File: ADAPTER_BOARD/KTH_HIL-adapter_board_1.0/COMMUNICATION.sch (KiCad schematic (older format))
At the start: 15 parts, among them U1 SN65HVD233, U2 SN65HVD233

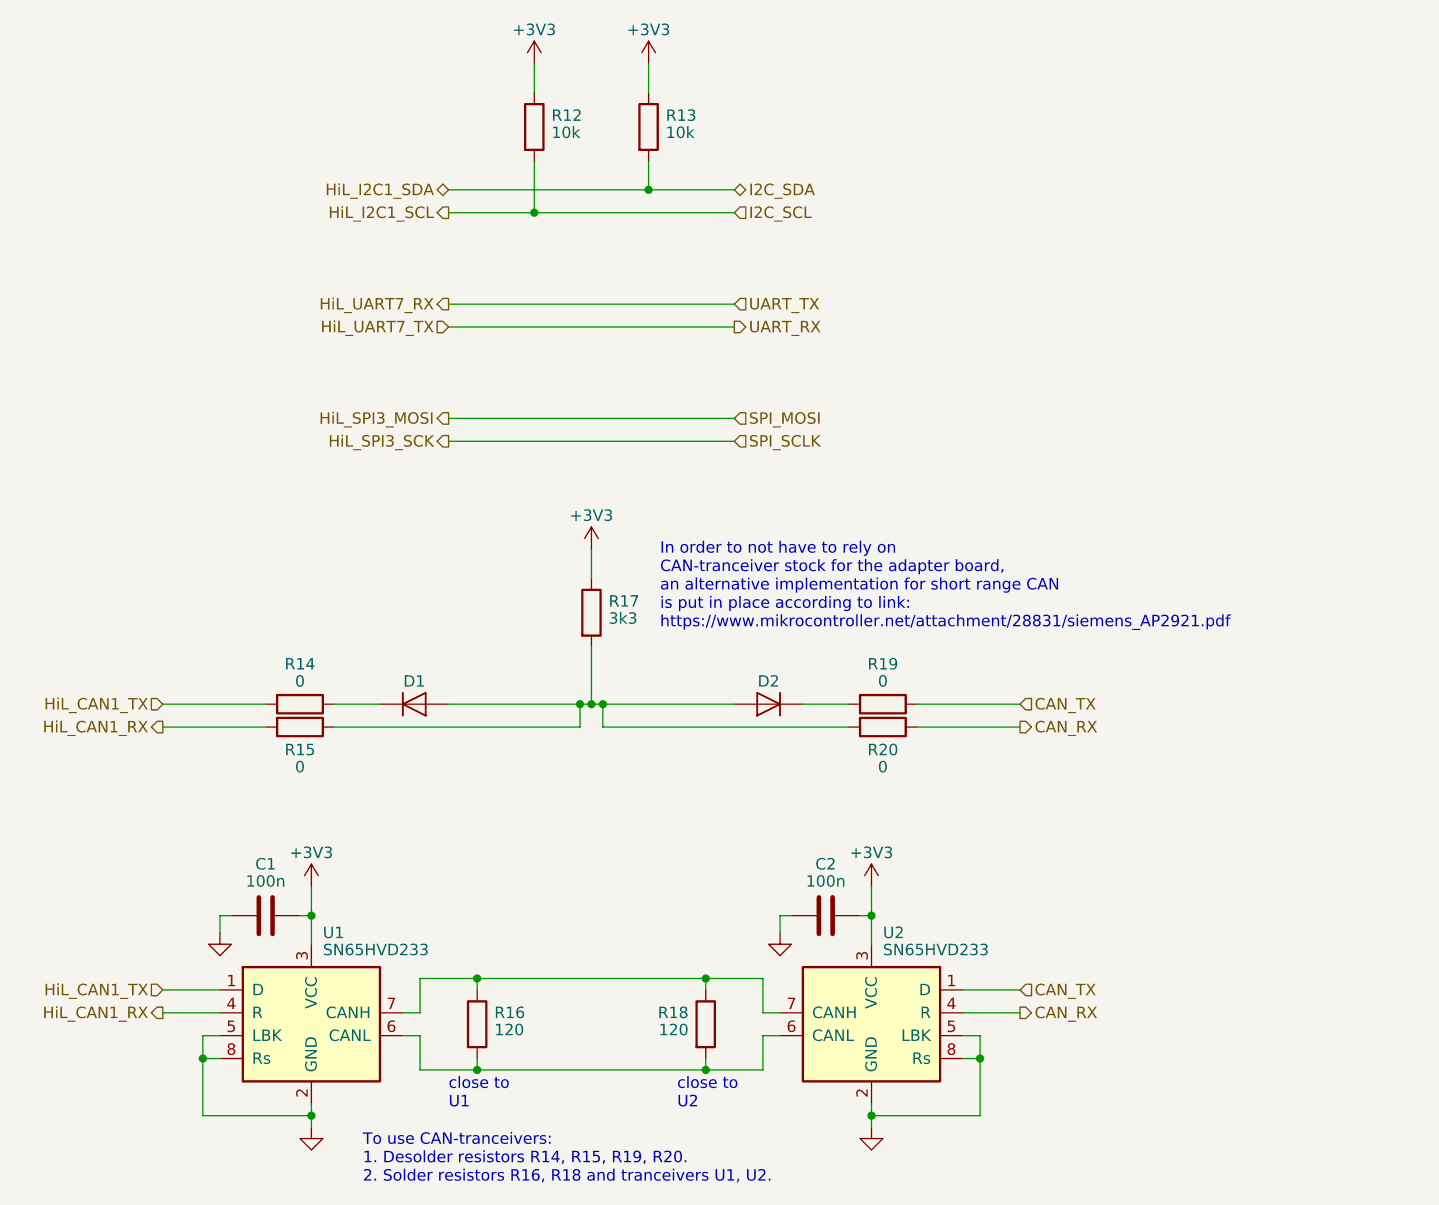
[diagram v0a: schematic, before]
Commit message: Fixed comments regarding schematic
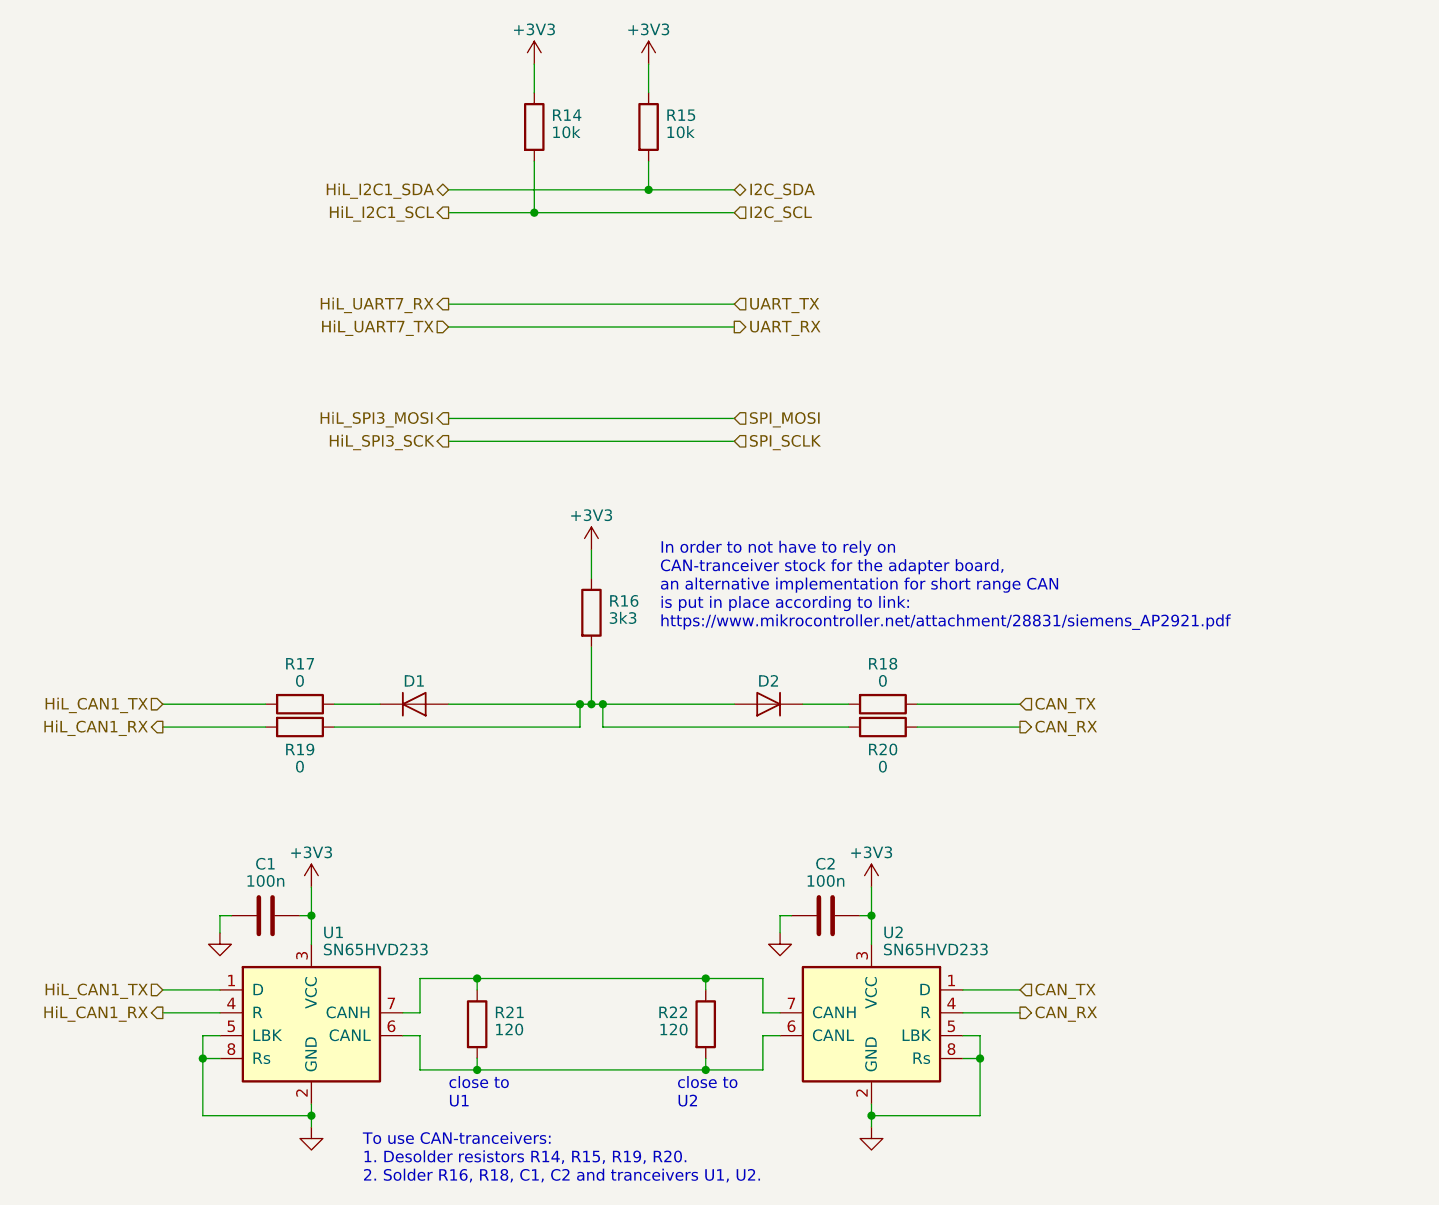
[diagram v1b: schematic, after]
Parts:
- renumbered R12 to R14, R13 to R15, R17 to R16, R14 to R17, R19 to R18, R15 to R19, R16 to R21, R18 to R22
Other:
- note added: "To use CAN-tranceivers:\n1. Desolder resistors R14, R15, R19, R20. \n2. Solder R16, R18, C1, C2 and tranceivers U1, U2."
- note removed: "To use CAN-tranceivers:\n1. Desolder resistors R14, R15, R19, R20. \n2. Solder resistors R16, R18 and tranceivers U1, U2."
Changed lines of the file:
@@
 EESchema Schematic File Version 4
-LIBS:HIL_ADAPTER_BOARD-cache
 EELAYER 30 0
 EELAYER END
@@
 CAN_RX
 $Comp
-L Device:R R13
+L Device:R R15
 U 1 1 635BC85D
 P 6125 1475
-F 0 "R13" H 6200 1525 50  0000 L CNN
+F 0 "R15" H 6200 1525 50  0000 L CNN
 F 1 "10k" H 6200 1450 50  0000 L CNN
 F 2 "Resistor_SMD:R_0603_1608Metric" V 6055 1475 50  0001 C CNN
@@
 $EndComp
 $Comp
-L Device:R R12
+L Device:R R14
 U 1 1 635BD521
 P 5625 1475
-F 0 "R12" H 5700 1525 50  0000 L CNN
+F 0 "R14" H 5700 1525 50  0000 L CNN
 F 1 "10k" H 5700 1450 50  0000 L CNN
 F 2 "Resistor_SMD:R_0603_1608Metric" V 5555 1475 50  0001 C CNN
@@
 	5250 2350 6500 2350
 $Comp
-L Device:R R17
+L Device:R R16
 U 1 1 6367642B
 P 5875 3600
-F 0 "R17" H 5950 3650 50  0000 L CNN
+F 0 "R16" H 5950 3650 50  0000 L CNN
 F 1 "3k3" H 5950 3575 50  0000 L CNN
 F 2 "Resistor_SMD:R_0603_1608Metric" V 5805 3600 50  0001 C CNN
@@
 $EndComp
 $Comp
-L Device:R R18
+L Device:R R22
 U 1 1 636B11A6
 P 6375 5400
-F 0 "R18" H 6300 5450 50  0000 R CNN
+F 0 "R22" H 6300 5450 50  0000 R CNN
 F 1 "120" H 6300 5375 50  0000 R CNN
 F 2 "Resistor_SMD:R_0603_1608Metric" V 6305 5400 50  0001 C CNN
@@
 $EndComp
 $Comp
-L Device:R R16
+L Device:R R21
 U 1 1 636B2601
 P 5375 5400
-F 0 "R16" H 5450 5450 50  0000 L CNN
+F 0 "R21" H 5450 5450 50  0000 L CNN
 F 1 "120" H 5450 5375 50  0000 L CNN
 F 2 "Resistor_SMD:R_0603_1608Metric" V 5305 5400 50  0001 C CNN
@@
 	4000 5350 4250 5350
 $Comp
-L Device:R R19
+L Device:R R18
 U 1 1 636D715E
 P 7150 4000
-F 0 "R19" V 6975 4000 50  0000 C CNN
+F 0 "R18" V 6975 4000 50  0000 C CNN
 F 1 "0" V 7050 4000 50  0000 C CNN
 F 2 "Resistor_SMD:R_0603_1608Metric" V 7080 4000 50  0001 C CNN
@@
 $EndComp
 $Comp
-L Device:R R14
+L Device:R R17
 U 1 1 636DD8B0
 P 4600 4000
-F 0 "R14" V 4425 4000 50  0000 C CNN
+F 0 "R17" V 4425 4000 50  0000 C CNN
 F 1 "0" V 4500 4000 50  0000 C CNN
 F 2 "Resistor_SMD:R_0603_1608Metric" V 4530 4000 50  0001 C CNN
@@
 $EndComp
 $Comp
-L Device:R R15
+L Device:R R19
 U 1 1 636DD8B6
 P 4600 4100
-F 0 "R15" V 4700 4100 50  0000 C CNN
+F 0 "R19" V 4700 4100 50  0000 C CNN
 F 1 "0" V 4775 4100 50  0000 C CNN
 F 2 "Resistor_SMD:R_0603_1608Metric" V 4530 4100 50  0001 C CNN
@@
 	4450 4100 4000 4100
 Text Notes 4875 6100 0    50   ~ 0
-To use CAN-tranceivers:\n1. Desolder resistors R14, R15, R19, R20. \n2. Solder resistors R16, R18 and tranceivers U1, U2.
+To use CAN-tranceivers:\n1. Desolder resistors R14, R15, R19, R20. \n2. Solder R16, R18, C1, C2 and tranceivers U1, U2.
 Text HLabel 5250 2750 0    50   Output ~ 0
 HiL_SPI3_MOSI
